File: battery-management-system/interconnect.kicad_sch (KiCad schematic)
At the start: 0 parts

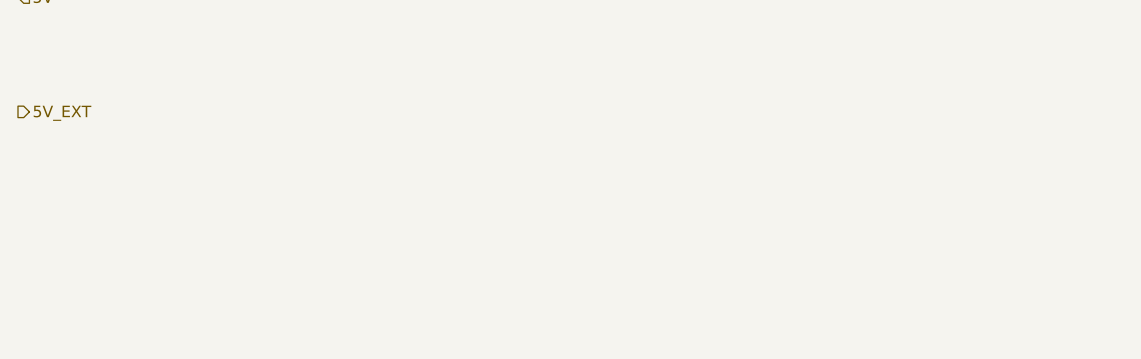
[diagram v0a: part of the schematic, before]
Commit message: define basic hierarchy and power supplies
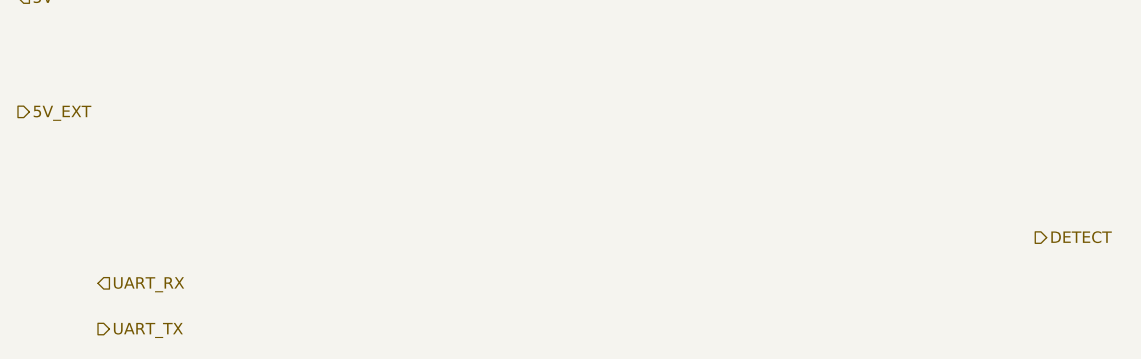
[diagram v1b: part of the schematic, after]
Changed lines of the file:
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@@
 (kicad_sch (version 20211123) (generator eeschema)
   (paper "A4")
+  (hierarchical_label "DETECT" (shape output) (at 198.12 82.55 0)
+    (effects (font (size 1.27 1.27)) (justify left))
+  )
   (hierarchical_label "5V" (shape input) (at 85.09 55.88 0)
     (effects (font (size 1.27 1.27)) (justify left))
   )
+  (hierarchical_label "UART_TX" (shape output) (at 93.98 92.71 0)
+    (effects (font (size 1.27 1.27)) (justify left))
+  )
+  (hierarchical_label "UART_RX" (shape input) (at 93.98 87.63 0)
+    (effects (font (size 1.27 1.27)) (justify left))
+  )

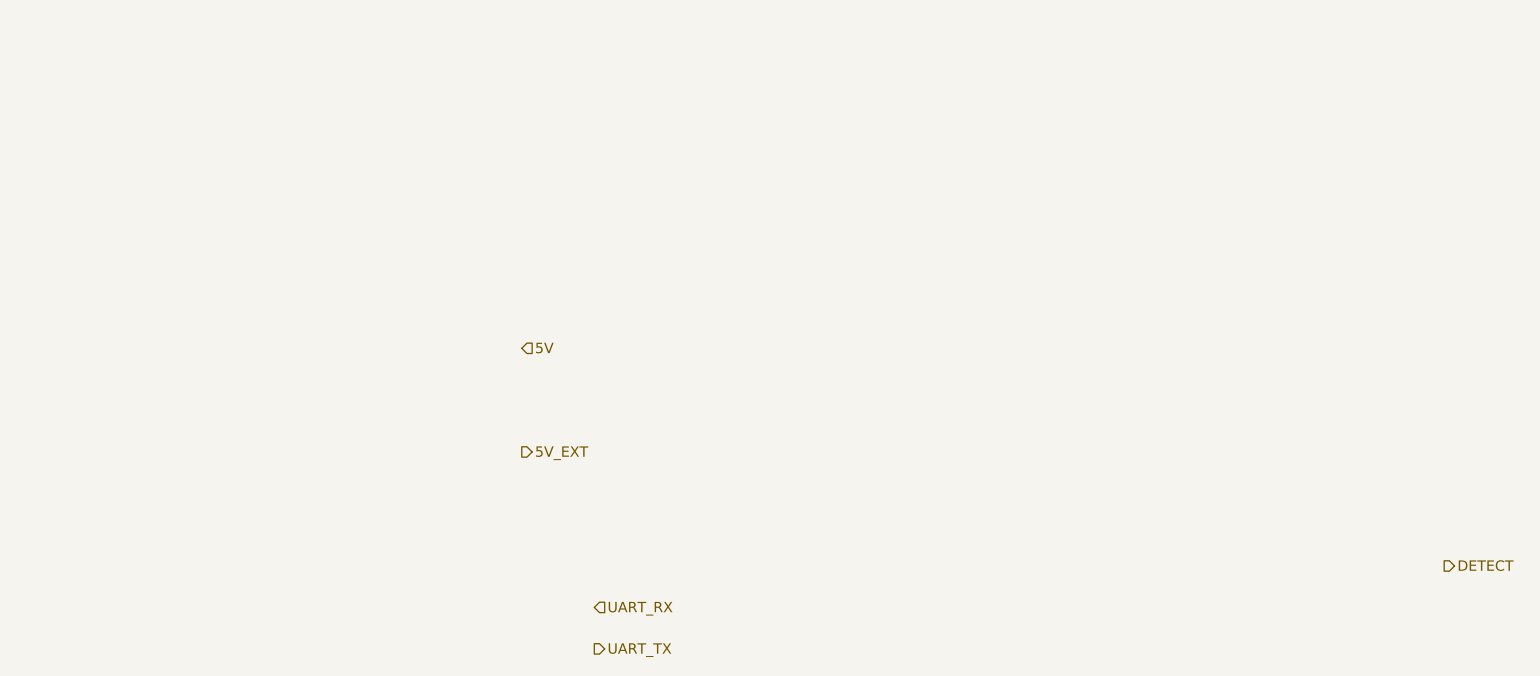
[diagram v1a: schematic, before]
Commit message: implement interconnect
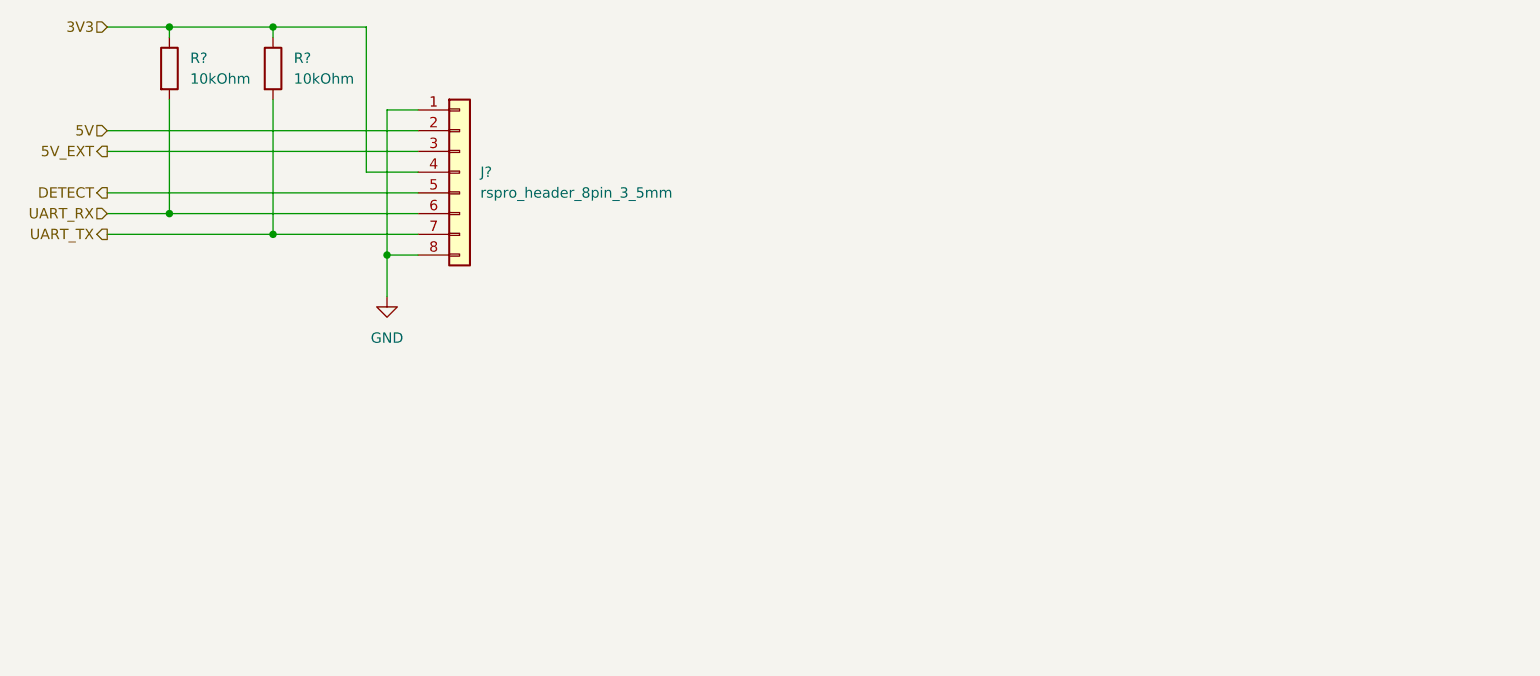
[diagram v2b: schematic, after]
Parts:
- added J?: rspro_header_8pin_3_5mm, benediktibk:rspro_header_8pin_3_5mm, symbol benediktibk:rspro_header_8pin_3_5mm
- added R? (x2): 10kOhm, benediktibk:R_0603_1608Metric_Pad0.98x0.95mm_HandSolder, symbol benediktibk:R_10kOhm_SMD_0603_100mW_1%
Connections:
- net 5V: now also J?.2 (Pin_2)
- net 5V_EXT: now also J?.3 (Pin_3)
- net DETECT: now also J?.5 (Pin_5)
- net UART_RX: now also J?.6 (Pin_6), R?.2
- net UART_TX: now also J?.7 (Pin_7), R?.2
- new net 3V3: J?.4 (Pin_4), R?.1, R?.1
- new net GND: J?.1 (Pin_1), J?.8 (Pin_8)
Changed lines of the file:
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@@
 (kicad_sch (version 20211123) (generator eeschema)
   (paper "A4")
-  (hierarchical_label "DETECT" (shape output) (at 198.12 82.55 0)
-    (effects (font (size 1.27 1.27)) (justify left))
+  (junction (at 54.61 16.51) (diameter 0) (color 0 0 0 0)
   )
-  (hierarchical_label "5V" (shape input) (at 85.09 55.88 0)
-    (effects (font (size 1.27 1.27)) (justify left))
+  (junction (at 41.91 39.37) (diameter 0) (color 0 0 0 0)
   )
-  (hierarchical_label "UART_TX" (shape output) (at 93.98 92.71 0)
-    (effects (font (size 1.27 1.27)) (justify left))
+  (junction (at 68.58 44.45) (diameter 0) (color 0 0 0 0)
   )
-  (hierarchical_label "UART_RX" (shape input) (at 93.98 87.63 0)
-    (effects (font (size 1.27 1.27)) (justify left))
+  (junction (at 41.91 16.51) (diameter 0) (color 0 0 0 0)
   )
-  (hierarchical_label "5V_EXT" (shape output) (at 85.09 68.58 0)
-    (effects (font (size 1.27 1.27)) (justify left))
+  (junction (at 54.61 41.91) (diameter 0) (color 0 0 0 0)
+  )
+  (wire (pts (xy 68.58 44.45) (xy 72.39 44.45))
+    (stroke (width 0) (type default) (color 0 0 0 0))
+  )
+  (wire (pts (xy 68.58 26.67) (xy 68.58 44.45))
+    (stroke (width 0) (type default) (color 0 0 0 0))
+  )
+  (wire (pts (xy 66.04 16.51) (xy 54.61 16.51))
+    (stroke (width 0) (type default) (color 0 0 0 0))
+  )
+  (wire (pts (xy 66.04 34.29) (xy 66.04 16.51))
+    (stroke (width 0) (type default) (color 0 0 0 0))
+  )
+  (wire (pts (xy 34.29 39.37) (xy 41.91 39.37))
+    (stroke (width 0) (type default) (color 0 0 0 0))
+  )
+  (wire (pts (xy 68.58 44.45) (xy 68.58 49.53))
+    (stroke (width 0) (type default) (color 0 0 0 0))
+  )
+  (wire (pts (xy 54.61 16.51) (xy 54.61 17.78))
+    (stroke (width 0) (type default) (color 0 0 0 0))
+  )
+  (wire (pts (xy 34.29 29.21) (xy 72.39 29.21))
+    (stroke (width 0) (type default) (color 0 0 0 0))
+  )
+  (wire (pts (xy 72.39 26.67) (xy 68.58 26.67))
+    (stroke (width 0) (type default) (color 0 0 0 0))
+  )
+  (wire (pts (xy 41.91 16.51) (xy 41.91 17.78))
+    (stroke (width 0) (type default) (color 0 0 0 0))
+  )
+  (wire (pts (xy 34.29 31.75) (xy 72.39 31.75))
+    (stroke (width 0) (type default) (color 0 0 0 0))
+  )
+  (wire (pts (xy 41.91 39.37) (xy 72.39 39.37))
+    (stroke (width 0) (type default) (color 0 0 0 0))
+  )
+  (wire (pts (xy 54.61 41.91) (xy 72.39 41.91))
+    (stroke (width 0) (type default) (color 0 0 0 0))
+  )
+  (wire (pts (xy 72.39 34.29) (xy 66.04 34.29))
+    (stroke (width 0) (type default) (color 0 0 0 0))
+  )
+  (wire (pts (xy 41.91 25.4) (xy 41.91 39.37))
+    (stroke (width 0) (type default) (color 0 0 0 0))
+  )
+  (wire (pts (xy 34.29 41.91) (xy 54.61 41.91))
+    (stroke (width 0) (type default) (color 0 0 0 0))
+  )
+  (wire (pts (xy 54.61 16.51) (xy 41.91 16.51))
+    (stroke (width 0) (type default) (color 0 0 0 0))
+  )
+  (wire (pts (xy 41.91 16.51) (xy 34.29 16.51))
+    (stroke (width 0) (type default) (color 0 0 0 0))
+  )
+  (wire (pts (xy 34.29 36.83) (xy 72.39 36.83))
+    (stroke (width 0) (type default) (color 0 0 0 0))
+  )
+  (wire (pts (xy 54.61 25.4) (xy 54.61 41.91))
+    (stroke (width 0) (type default) (color 0 0 0 0))
+  )
+  (hierarchical_label "DETECT" (shape output) (at 34.29 36.83 180)
+    (effects (font (size 1.27 1.27)) (justify right))
+  )
+  (hierarchical_label "5V" (shape input) (at 34.29 29.21 180)
+    (effects (font (size 1.27 1.27)) (justify right))
+  )
+  (hierarchical_label "3V3" (shape input) (at 34.29 16.51 180)
+    (effects (font (size 1.27 1.27)) (justify right))
+  )
+  (hierarchical_label "UART_TX" (shape output) (at 34.29 41.91 180)
+    (effects (font (size 1.27 1.27)) (justify right))
+  )
+  (hierarchical_label "UART_RX" (shape input) (at 34.29 39.37 180)
+    (effects (font (size 1.27 1.27)) (justify right))
+  )
+  (hierarchical_label "5V_EXT" (shape output) (at 34.29 31.75 180)
+    (effects (font (size 1.27 1.27)) (justify right))
+  )
+  (symbol (lib_id "benediktibk:rspro_header_8pin_3_5mm") (at 77.47 34.29 0) (unit 1)
+    (in_bom yes) (on_board yes) (fields_autoplaced)
+    (property "Reference" "J?" (id 0) (at 80.01 34.2899 0)
+      (effects (font (size 1.27 1.27)) (justify left))
+    )
+    (property "Value" "rspro_header_8pin_3_5mm" (id 1) (at 80.01 36.8299 0)
+      (effects (font (size 1.27 1.27)) (justify left))
+    )
+    (property "Footprint" "benediktibk:rspro_header_8pin_3_5mm" (id 2) (at 77.47 34.29 0)
+      (effects (font (size 1.27 1.27)) hide)
+    )
+    (property "Datasheet" "~" (id 3) (at 77.47 34.29 0)
+      (effects (font (size 1.27 1.27)) hide)
+    )
+    (property "RS order number" "897-1048" (id 4) (at 77.47 34.29 0)
+      (effects (font (size 1.27 1.27)) hide)
+    )
+    (pin "1")
+    (pin "2")
+    (pin "3")
+    (pin "4")
+    (pin "5")
+    (pin "6")
+    (pin "7")
+    (pin "8")
+  )
+  (symbol (lib_id "benediktibk:R_10kOhm_SMD_0603_100mW_1%") (at 41.91 21.59 0) (unit 1)
+    (in_bom yes) (on_board yes) (fields_autoplaced)
+    (property "Reference" "R?" (id 0) (at 44.45 20.3199 0)
+      (effects (font (size 1.27 1.27)) (justify left))
+    )
+    (property "Value" "10kOhm" (id 1) (at 44.45 22.8599 0)
+      (effects (font (size 1.27 1.27)) (justify left))
+    )
+    (property "Footprint" "benediktibk:R_0603_1608Metric_Pad0.98x0.95mm_HandSolder" (id 2) (at 31.75 21.082 90)
+      (effects (font (size 1.27 1.27)) hide)
+    )
+    (property "Datasheet" "~" (id 3) (at 41.91 21.59 0)
+      (effects (font (size 1.27 1.27)) hide)
+    )
+    (property "RS order number" "125-1173" (id 4) (at 24.13 20.32 0)
+      (effects (font (size 1.27 1.27)) hide)
+    )
+    (pin "1")
+    (pin "2")
+  )
+  (symbol (lib_id "power:GND") (at 68.58 49.53 0) (unit 1)
+    (in_bom yes) (on_board yes) (fields_autoplaced)
+    (property "Reference" "#PWR?" (id 0) (at 68.58 55.88 0)
+      (effects (font (size 1.27 1.27)) hide)
+    )
+    (property "Value" "GND" (id 1) (at 68.58 54.61 0))
+    (property "Footprint" "" (id 2) (at 68.58 49.53 0)
+      (effects (font (size 1.27 1.27)) hide)
+    )
+    (property "Datasheet" "" (id 3) (at 68.58 49.53 0)
+      (effects (font (size 1.27 1.27)) hide)
+    )
+    (pin "1")
+  )
+  (symbol (lib_id "benediktibk:R_10kOhm_SMD_0603_100mW_1%") (at 54.61 21.59 0) (unit 1)
+    (in_bom yes) (on_board yes) (fields_autoplaced)
+    (property "Reference" "R?" (id 0) (at 57.15 20.3199 0)
+      (effects (font (size 1.27 1.27)) (justify left))
+    )
+    (property "Value" "10kOhm" (id 1) (at 57.15 22.8599 0)
+      (effects (font (size 1.27 1.27)) (justify left))
+    )
+    (property "Footprint" "benediktibk:R_0603_1608Metric_Pad0.98x0.95mm_HandSolder" (id 2) (at 44.45 21.082 90)
+      (effects (font (size 1.27 1.27)) hide)
+    )
+    (property "Datasheet" "~" (id 3) (at 54.61 21.59 0)
+      (effects (font (size 1.27 1.27)) hide)
+    )
+    (property "RS order number" "125-1173" (id 4) (at 36.83 20.32 0)
+      (effects (font (size 1.27 1.27)) hide)
+    )
+    (pin "1")
+    (pin "2")
   )
 )

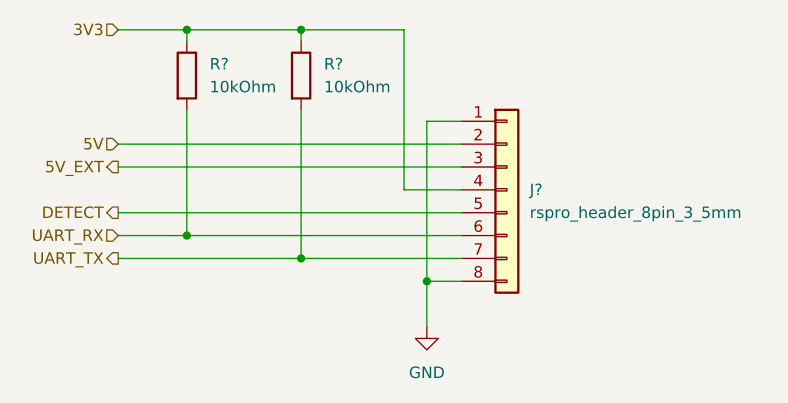
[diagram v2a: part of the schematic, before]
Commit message: route UART and ADC channels on MCU
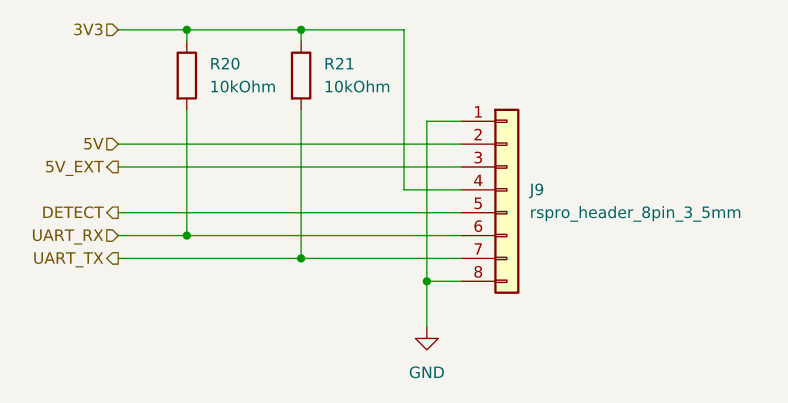
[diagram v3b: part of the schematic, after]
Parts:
- gave numbers to parts that had none: 3
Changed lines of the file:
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@@
   (symbol (lib_id "benediktibk:rspro_header_8pin_3_5mm") (at 77.47 34.29 0) (unit 1)
     (in_bom yes) (on_board yes) (fields_autoplaced)
-    (property "Reference" "J?" (id 0) (at 80.01 34.2899 0)
+    (property "Reference" "J9" (id 0) (at 80.01 34.2899 0)
       (effects (font (size 1.27 1.27)) (justify left))
     )
@@
   (symbol (lib_id "benediktibk:R_10kOhm_SMD_0603_100mW_1%") (at 41.91 21.59 0) (unit 1)
     (in_bom yes) (on_board yes) (fields_autoplaced)
-    (property "Reference" "R?" (id 0) (at 44.45 20.3199 0)
+    (property "Reference" "R20" (id 0) (at 44.45 20.3199 0)
       (effects (font (size 1.27 1.27)) (justify left))
     )
@@
   (symbol (lib_id "power:GND") (at 68.58 49.53 0) (unit 1)
     (in_bom yes) (on_board yes) (fields_autoplaced)
-    (property "Reference" "#PWR?" (id 0) (at 68.58 55.88 0)
+    (property "Reference" "#PWR0127" (id 0) (at 68.58 55.88 0)
       (effects (font (size 1.27 1.27)) hide)
     )
@@
   (symbol (lib_id "benediktibk:R_10kOhm_SMD_0603_100mW_1%") (at 54.61 21.59 0) (unit 1)
     (in_bom yes) (on_board yes) (fields_autoplaced)
-    (property "Reference" "R?" (id 0) (at 57.15 20.3199 0)
+    (property "Reference" "R21" (id 0) (at 57.15 20.3199 0)
       (effects (font (size 1.27 1.27)) (justify left))
     )

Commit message: add components
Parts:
- removed J9: rspro_header_8pin_3_5mm, benediktibk:rspro_header_8pin_3_5mm, symbol benediktibk:rspro_header_8pin_3_5mm
- added J9: rspro_header_5pin_3_5mm, benediktibk:rspro_header_5pin_3_5mm, symbol benediktibk:rspro_header_5pin_3_5mm
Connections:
- net 5V: now also J9.2 (Pin_2)
- net 5V_EXT: now also J9.3 (Pin_3)
- net GND: now also J9.1 (Pin_1)
- net UART_RX: now also J9.4 (Pin_4)
- net UART_TX: now also J9.5 (Pin_5)

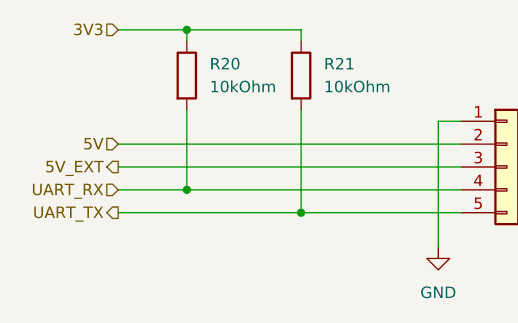
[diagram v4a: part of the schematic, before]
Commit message: add balancing sheet
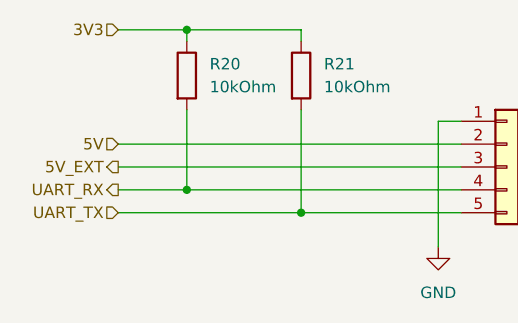
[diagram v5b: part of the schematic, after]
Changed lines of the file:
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@@
     (effects (font (size 1.27 1.27)) (justify right))
   )
-  (hierarchical_label "UART_TX" (shape output) (at 34.29 36.83 180) (fields_autoplaced)
+  (hierarchical_label "UART_TX" (shape input) (at 34.29 36.83 180) (fields_autoplaced)
     (effects (font (size 1.27 1.27)) (justify right))
   )
-  (hierarchical_label "UART_RX" (shape input) (at 34.29 34.29 180) (fields_autoplaced)
+  (hierarchical_label "UART_RX" (shape output) (at 34.29 34.29 180) (fields_autoplaced)
     (effects (font (size 1.27 1.27)) (justify right))
   )

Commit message: improve layout
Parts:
- renumbered J9 to J21, R20 to R43, R21 to R44
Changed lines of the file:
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@@
   (symbol (lib_id "benediktibk:R_10kOhm_SMD_0603_100mW_1%") (at 41.91 21.59 0) (unit 1)
     (in_bom yes) (on_board yes) (dnp no) (fields_autoplaced)
-    (property "Reference" "R20" (at 44.45 20.3199 0)
+    (property "Reference" "R43" (at 44.45 20.3199 0)
       (effects (font (size 1.27 1.27)) (justify left))
     )
@@
       (project "battery-management-system"
         (path "/5272f0ff-3069-41a9-bca2-80beede8b4b2/3df28b0f-4877-411d-a6e0-0c6dff0863b2"
-          (reference "R20") (unit 1)
+          (reference "R43") (unit 1)
         )
       )
@@
   (symbol (lib_id "benediktibk:rspro_header_5pin_3_5mm") (at 77.47 31.75 0) (unit 1)
     (in_bom yes) (on_board yes) (dnp no) (fields_autoplaced)
-    (property "Reference" "J9" (at 80.01 30.48 0)
+    (property "Reference" "J21" (at 80.01 30.48 0)
       (effects (font (size 1.27 1.27)) (justify left))
     )
@@
       (project "battery-management-system"
         (path "/5272f0ff-3069-41a9-bca2-80beede8b4b2/3df28b0f-4877-411d-a6e0-0c6dff0863b2"
-          (reference "J9") (unit 1)
+          (reference "J21") (unit 1)
         )
       )
@@
   (symbol (lib_id "power:GND") (at 69.85 40.64 0) (unit 1)
     (in_bom yes) (on_board yes) (dnp no) (fields_autoplaced)
-    (property "Reference" "#PWR0127" (at 69.85 46.99 0)
+    (property "Reference" "#PWR067" (at 69.85 46.99 0)
       (effects (font (size 1.27 1.27)) hide)
     )
@@
       (project "battery-management-system"
         (path "/5272f0ff-3069-41a9-bca2-80beede8b4b2/3df28b0f-4877-411d-a6e0-0c6dff0863b2"
-          (reference "#PWR0127") (unit 1)
+          (reference "#PWR067") (unit 1)
         )
       )
@@
   (symbol (lib_id "benediktibk:R_10kOhm_SMD_0603_100mW_1%") (at 54.61 21.59 0) (unit 1)
     (in_bom yes) (on_board yes) (dnp no) (fields_autoplaced)
-    (property "Reference" "R21" (at 57.15 20.3199 0)
+    (property "Reference" "R44" (at 57.15 20.3199 0)
       (effects (font (size 1.27 1.27)) (justify left))
     )
@@
       (project "battery-management-system"
         (path "/5272f0ff-3069-41a9-bca2-80beede8b4b2/3df28b0f-4877-411d-a6e0-0c6dff0863b2"
-          (reference "R21") (unit 1)
+          (reference "R44") (unit 1)
         )
       )
